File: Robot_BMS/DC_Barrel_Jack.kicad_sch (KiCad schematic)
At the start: 3 parts, among them J5 694108301002

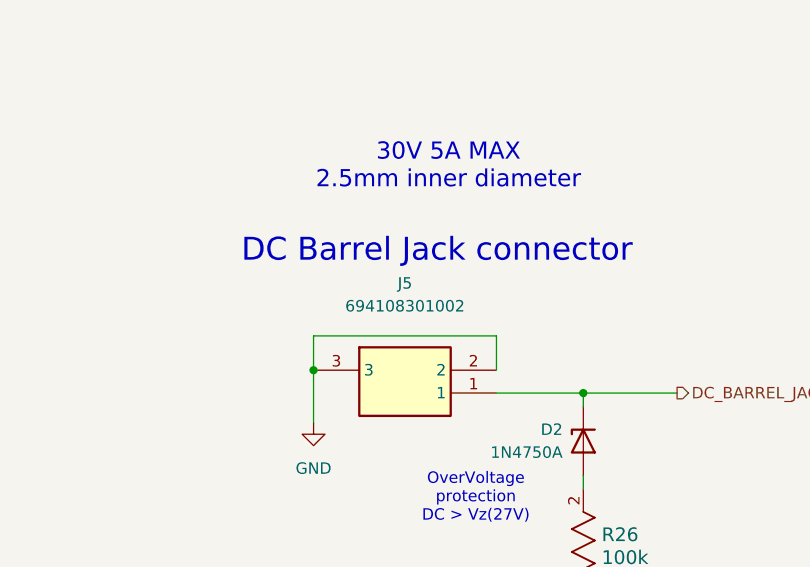
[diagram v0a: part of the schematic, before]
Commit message: creation of seperate 4 layer pcb for individual technical report
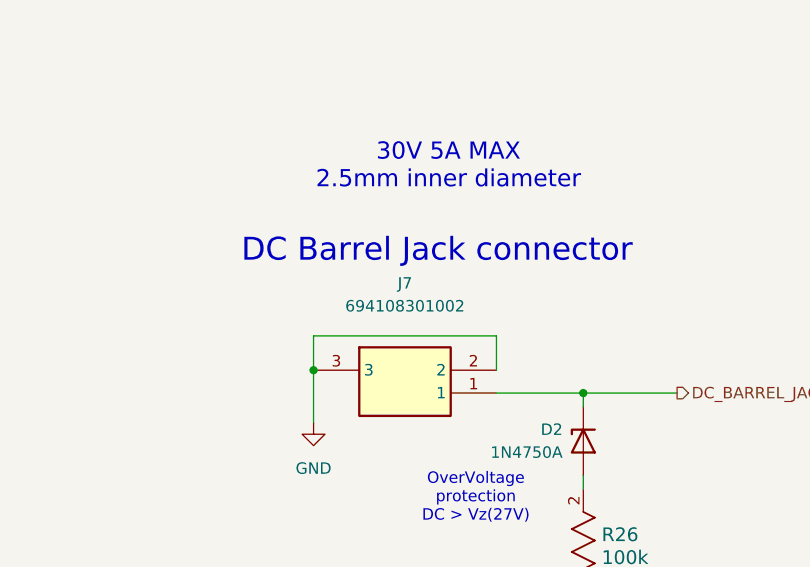
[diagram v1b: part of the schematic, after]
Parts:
- renumbered J5 to J7
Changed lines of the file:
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@@
 		(dnp no)
 		(fields_autoplaced yes)
-		(property "Reference" "#PWR037"
+		(property "Reference" "#PWR038"
 			(at 164.592 136.652 0)
 			(effects
@@
 			(project "Robot_BMS"
 				(path "/72551b1c-3d40-4199-8911-e5b015f4abec/7a60a594-7330-4ecb-a3c9-8c0f96aa21b4"
-					(reference "#PWR037")
+					(reference "#PWR038")
 					(unit 1)
 				)
@@
 		(dnp no)
 		(fields_autoplaced yes)
-		(property "Reference" "#PWR036"
+		(property "Reference" "#PWR037"
 			(at 134.62 115.316 0)
 			(effects
@@
 			(project "Robot_BMS"
 				(path "/72551b1c-3d40-4199-8911-e5b015f4abec/7a60a594-7330-4ecb-a3c9-8c0f96aa21b4"
-					(reference "#PWR036")
+					(reference "#PWR037")
 					(unit 1)
 				)
@@
 		(on_board yes)
 		(dnp no)
-		(property "Reference" "J5"
+		(property "Reference" "J7"
 			(at 144.78 93.472 0)
 			(effects
@@
 			(project ""
 				(path "/72551b1c-3d40-4199-8911-e5b015f4abec/7a60a594-7330-4ecb-a3c9-8c0f96aa21b4"
-					(reference "J5")
+					(reference "J7")
 					(unit 1)
 				)

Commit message: halfway throgh battery management pcb layout
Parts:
- renumbered J7 to J8, R26 to R27
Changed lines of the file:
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@@
 		(dnp no)
 		(fields_autoplaced yes)
-		(property "Reference" "#PWR038"
+		(property "Reference" "#PWR040"
 			(at 164.592 136.652 0)
 			(effects
@@
 			(project "Robot_BMS"
 				(path "/72551b1c-3d40-4199-8911-e5b015f4abec/7a60a594-7330-4ecb-a3c9-8c0f96aa21b4"
-					(reference "#PWR038")
+					(reference "#PWR040")
 					(unit 1)
 				)
@@
 		(dnp no)
 		(fields_autoplaced yes)
-		(property "Reference" "#PWR037"
+		(property "Reference" "#PWR039"
 			(at 134.62 115.316 0)
 			(effects
@@
 			(project "Robot_BMS"
 				(path "/72551b1c-3d40-4199-8911-e5b015f4abec/7a60a594-7330-4ecb-a3c9-8c0f96aa21b4"
-					(reference "#PWR037")
+					(reference "#PWR039")
 					(unit 1)
 				)
@@
 		(on_board yes)
 		(dnp no)
-		(property "Reference" "J7"
+		(property "Reference" "J8"
 			(at 144.78 93.472 0)
 			(effects
@@
 		)
 		(property "Price" "0.804"
+			(at 134.62 103.124 0)
+			(effects
+				(font
+					(size 1.27 1.27)
+				)
+				(hide yes)
+			)
+		)
+		(property "Chip1Stop Part Number" ""
+			(at 134.62 103.124 0)
+			(effects
+				(font
+					(size 1.27 1.27)
+				)
+				(hide yes)
+			)
+		)
+		(property "Chip1Stop Price/Stock" ""
 			(at 134.62 103.124 0)
 			(effects
@@
 			(project ""
 				(path "/72551b1c-3d40-4199-8911-e5b015f4abec/7a60a594-7330-4ecb-a3c9-8c0f96aa21b4"
-					(reference "J7")
+					(reference "J8")
 					(unit 1)
 				)
@@
 			)
 		)
+		(property "Chip1Stop Part Number" ""
+			(at 164.592 110.998 0)
+			(effects
+				(font
+					(size 1.27 1.27)
+				)
+				(hide yes)
+			)
+		)
+		(property "Chip1Stop Price/Stock" ""
+			(at 164.592 110.998 0)
+			(effects
+				(font
+					(size 1.27 1.27)
+				)
+				(hide yes)
+			)
+		)
 		(pin "2"
 		)
@@
 		(dnp no)
 		(fields_autoplaced yes)
-		(property "Reference" "R26"
+		(property "Reference" "R27"
 			(at 166.624 121.4119 90)
 			(effects
@@
 		(property "Manufacturer_Part_Number" "ESR03EZPF1003"
 			(at 164.592 129.032 90)
+			(effects
+				(font
+					(size 1.27 1.27)
+				)
+				(hide yes)
+			)
+		)
+		(property "Chip1Stop Part Number" ""
+			(at 164.592 129.032 0)
+			(effects
+				(font
+					(size 1.27 1.27)
+				)
+				(hide yes)
+			)
+		)
+		(property "Chip1Stop Price/Stock" ""
+			(at 164.592 129.032 0)
 			(effects
 				(font
@@
 			(project "Robot_BMS"
 				(path "/72551b1c-3d40-4199-8911-e5b015f4abec/7a60a594-7330-4ecb-a3c9-8c0f96aa21b4"
-					(reference "R26")
+					(reference "R27")
 					(unit 1)
 				)
